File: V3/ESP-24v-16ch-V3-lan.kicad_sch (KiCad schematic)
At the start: 28 parts, among them J7 ETHERNET, U5 LAN8710A

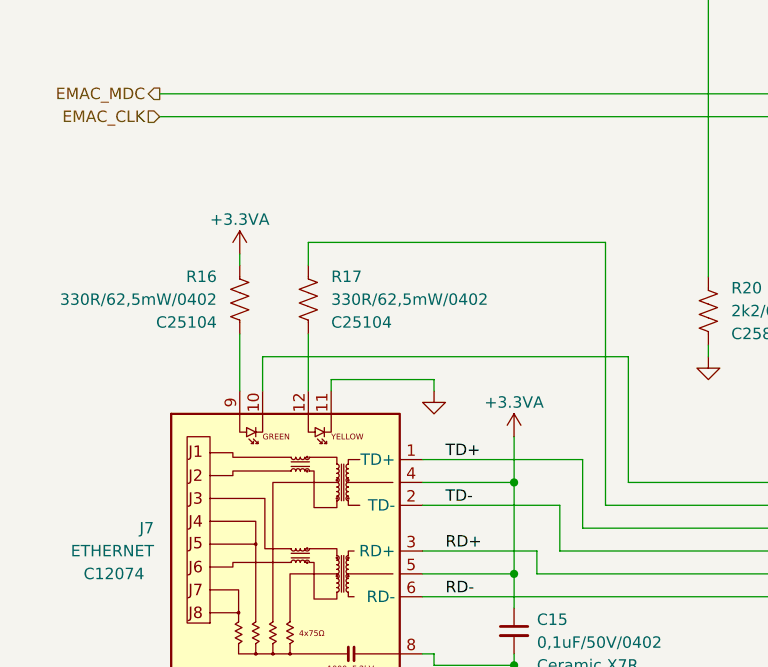
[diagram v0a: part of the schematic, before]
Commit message: Replaced R16 and R17 for a R-Pack
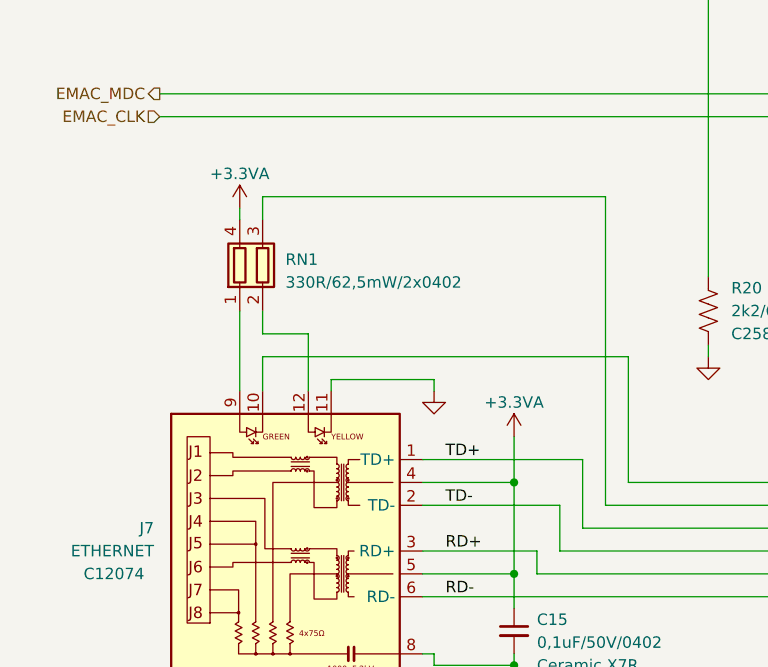
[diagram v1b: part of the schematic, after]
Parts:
- removed R16, R17: 330R/62,5mW/0402, Tales:R_0402_1005Metric, symbol Device:R_US
- added RN1: 330R/62,5mW/2x0402, Resistor_SMD:R_Array_Convex_2x0402, symbol Device:R_Pack02
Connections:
- net +3.3VA: now also RN1.4 (R1.2)
- net LED_Y_A: now also RN1.3 (R2.2)
- net at J7.12: now also RN1.2 (R2.1)
- net at J7.9: now also RN1.1 (R1.1)
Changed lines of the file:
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@@
     (stroke (width 0) (type default))
   )
-  (wire (pts (xy 83.82 123.19) (xy 83.82 152.4))
+  (wire (pts (xy 83.82 118.11) (xy 83.82 152.4))
     (stroke (width 0) (type default))
   )
@@
     (stroke (width 0) (type default))
   )
-  (wire (pts (xy 43.18 124.46) (xy 43.18 125.73))
+  (wire (pts (xy 43.18 119.38) (xy 43.18 120.65))
     (stroke (width 0) (type default))
   )
@@
     (stroke (width 0) (type default))
   )
-  (wire (pts (xy 43.18 133.35) (xy 43.18 139.7))
+  (wire (pts (xy 43.18 130.81) (xy 43.18 139.7))
     (stroke (width 0) (type default))
   )
@@
     (stroke (width 0) (type default))
   )
+  (wire (pts (xy 45.72 133.35) (xy 50.8 133.35))
+    (stroke (width 0) (type default))
+  )
   (wire (pts (xy 151.13 25.4) (xy 151.13 29.21))
     (stroke (width 0) (type default))
@@
     (stroke (width 0) (type default))
   )
+  (wire (pts (xy 45.72 130.81) (xy 45.72 133.35))
+    (stroke (width 0) (type default))
+  )
   (wire (pts (xy 63.5 152.4) (xy 78.74 152.4))
     (stroke (width 0) (type default))
@@
     (stroke (width 0) (type default))
   )
-  (wire (pts (xy 50.8 123.19) (xy 83.82 123.19))
+  (wire (pts (xy 45.72 118.11) (xy 83.82 118.11))
     (stroke (width 0) (type default))
   )
@@
     (stroke (width 0) (type default))
   )
-  (wire (pts (xy 50.8 125.73) (xy 50.8 123.19))
+  (wire (pts (xy 45.72 120.65) (xy 45.72 118.11))
     (stroke (width 0) (type default))
   )
@@
         (path "/2bc5a21a-1d79-419d-a592-6852cc07b00a/c76fc600-a423-4f14-bc69-e86c7c986b21"
           (reference "#PWR060") (unit 1)
-        )
-      )
-    )
-  )
-  (symbol (lib_id "Device:R_US") (at 50.8 129.54 0) (unit 1)
-    (in_bom yes) (on_board yes) (dnp no)
-    (property "Reference" "R17" (at 53.34 127 0)
-      (effects (font (size 1.27 1.27)) (justify left))
-    )
-    (property "Value" "330R/62,5mW/0402" (at 53.34 129.54 0)
-      (effects (font (size 1.27 1.27)) (justify left))
-    )
-    (property "Footprint" "Tales:R_0402_1005Metric" (at 51.816 129.794 90)
-      (effects (font (size 1.27 1.27)) hide)
-    )
-    (property "Datasheet" "~" (at 50.8 129.54 0)
-      (effects (font (size 1.27 1.27)) hide)
-    )
-    (property "Case" "0402/1005" (at 50.8 129.54 0)
-      (effects (font (size 1.27 1.27)) hide)
-    )
-    (property "Mfr" "Uniroyal" (at 50.8 129.54 0)
-      (effects (font (size 1.27 1.27)) hide)
-    )
-    (property "Vendor" "JLCPCB" (at 50.8 129.54 0)
-      (effects (font (size 1.27 1.27)) hide)
-    )
-    (property "Mfr PN" "0402WGF3300TCE" (at 50.8 129.54 0)
-      (effects (font (size 1.27 1.27)) hide)
-    )
-    (property "Technology" "~" (at 50.8 129.54 0)
-      (effects (font (size 1.27 1.27)) hide)
-    )
-    (property "Vendor PN" "C25104" (at 50.8 129.54 0)
-      (effects (font (size 1.27 1.27)) hide)
-    )
-    (property "LCSC Part #" "C25104" (at 53.34 132.08 0)
-      (effects (font (size 1.27 1.27)) (justify left))
-    )
-    (property "JLCPCB BOM" "1" (at 50.8 129.54 0)
-      (effects (font (size 1.27 1.27)) hide)
-    )
-    (pin "1")
-    (pin "2")
-    (instances
-      (project "ESP-24v-16ch-V3"
-        (path "/2bc5a21a-1d79-419d-a592-6852cc07b00a/c76fc600-a423-4f14-bc69-e86c7c986b21"
-          (reference "R17") (unit 1)
         )
       )
@@
     )
   )
-  (symbol (lib_id "Device:R_US") (at 43.18 129.54 0) (unit 1)
-    (in_bom yes) (on_board yes) (dnp no)
-    (property "Reference" "R16" (at 40.64 127 0)
-      (effects (font (size 1.27 1.27)) (justify right))
-    )
-    (property "Value" "330R/62,5mW/0402" (at 40.64 129.54 0)
-      (effects (font (size 1.27 1.27)) (justify right))
-    )
-    (property "Footprint" "Tales:R_0402_1005Metric" (at 44.196 129.794 90)
-      (effects (font (size 1.27 1.27)) hide)
-    )
-    (property "Datasheet" "~" (at 43.18 129.54 0)
-      (effects (font (size 1.27 1.27)) hide)
-    )
-    (property "Case" "0402/1005" (at 43.18 129.54 0)
-      (effects (font (size 1.27 1.27)) hide)
-    )
-    (property "Mfr" "Uniroyal" (at 43.18 129.54 0)
-      (effects (font (size 1.27 1.27)) hide)
-    )
-    (property "Vendor" "JLCPCB" (at 43.18 129.54 0)
-      (effects (font (size 1.27 1.27)) hide)
-    )
-    (property "Mfr PN" "0402WGF3300TCE" (at 43.18 129.54 0)
-      (effects (font (size 1.27 1.27)) hide)
-    )
-    (property "Technology" "~" (at 43.18 129.54 0)
-      (effects (font (size 1.27 1.27)) hide)
-    )
-    (property "Vendor PN" "C25104" (at 43.18 129.54 0)
-      (effects (font (size 1.27 1.27)) hide)
-    )
-    (property "LCSC Part #" "C25104" (at 40.64 132.08 0)
-      (effects (font (size 1.27 1.27)) (justify right))
-    )
-    (property "JLCPCB BOM" "1" (at 43.18 129.54 0)
-      (effects (font (size 1.27 1.27)) hide)
-    )
-    (pin "1")
-    (pin "2")
-    (instances
-      (project "ESP-24v-16ch-V3"
-        (path "/2bc5a21a-1d79-419d-a592-6852cc07b00a/c76fc600-a423-4f14-bc69-e86c7c986b21"
-          (reference "R16") (unit 1)
-        )
-      )
-    )
-  )
   (symbol (lib_id "power:GND") (at 121.92 101.6 0) (unit 1)
     (in_bom yes) (on_board yes) (dnp no)
@@
         (path "/2bc5a21a-1d79-419d-a592-6852cc07b00a/c76fc600-a423-4f14-bc69-e86c7c986b21"
           (reference "#PWR059") (unit 1)
+        )
+      )
+    )
+  )
+  (symbol (lib_id "Device:R_Pack02") (at 45.72 125.73 0) (unit 1)
+    (in_bom yes) (on_board yes) (dnp no) (fields_autoplaced)
+    (property "Reference" "RN1" (at 48.26 125.095 0)
+      (effects (font (size 1.27 1.27)) (justify left))
+    )
+    (property "Value" "330R/62,5mW/2x0402" (at 48.26 127.635 0)
+      (effects (font (size 1.27 1.27)) (justify left))
+    )
+    (property "Footprint" "Resistor_SMD:R_Array_Convex_2x0402" (at 50.165 125.73 90)
+      (effects (font (size 1.27 1.27)) hide)
+    )
+    (property "Datasheet" "~" (at 45.72 125.73 0)
+      (effects (font (size 1.27 1.27)) hide)
+    )
+    (property "Case" "2x0402 Convex" (at 45.72 125.73 0)
+      (effects (font (size 1.27 1.27)) hide)
+    )
+    (property "JLCPCB BOM" "1" (at 45.72 125.73 0)
+      (effects (font (size 1.27 1.27)) hide)
+    )
+    (property "LCSC Part #" "C425334" (at 45.72 125.73 0)
+      (effects (font (size 1.27 1.27)) hide)
+    )
+    (property "Mfr" "Uniroyal" (at 45.72 125.73 0)
+      (effects (font (size 1.27 1.27)) hide)
+    )
+    (property "Mfr PN" "2D02WGJ0331TCE" (at 45.72 125.73 0)
+      (effects (font (size 1.27 1.27)) hide)
+    )
+    (property "Technology" "~" (at 45.72 125.73 0)
+      (effects (font (size 1.27 1.27)) hide)
+    )
+    (property "Vendor" "JLCPCB" (at 45.72 125.73 0)
+      (effects (font (size 1.27 1.27)) hide)
+    )
+    (property "Vendor PN" "C425334" (at 45.72 125.73 0)
+      (effects (font (size 1.27 1.27)) hide)
+    )
+    (pin "1")
+    (pin "2")
+    (pin "3")
+    (pin "4")
+    (instances
+      (project "ESP-24v-16ch-V3"
+        (path "/2bc5a21a-1d79-419d-a592-6852cc07b00a/c76fc600-a423-4f14-bc69-e86c7c986b21"
+          (reference "RN1") (unit 1)
         )
       )
@@
     )
   )
-  (symbol (lib_id "power:+3.3VA") (at 43.18 124.46 0) (unit 1)
-    (in_bom yes) (on_board yes) (dnp no)
-    (property "Reference" "#PWR037" (at 43.18 128.27 0)
-      (effects (font (size 1.27 1.27)) hide)
-    )
-    (property "Value" "+3.3VA" (at 43.18 120.65 0)
+  (symbol (lib_id "power:+3.3VA") (at 43.18 119.38 0) (unit 1)
+    (in_bom yes) (on_board yes) (dnp no)
+    (property "Reference" "#PWR037" (at 43.18 123.19 0)
+      (effects (font (size 1.27 1.27)) hide)
+    )
+    (property "Value" "+3.3VA" (at 43.18 115.57 0)
       (effects (font (size 1.27 1.27)))
     )
-    (property "Footprint" "" (at 43.18 124.46 0)
-      (effects (font (size 1.27 1.27)) hide)
-    )
-    (property "Datasheet" "" (at 43.18 124.46 0)
-      (effects (font (size 1.27 1.27)) hide)
-    )
+    (property "Footprint" "" (at 43.18 119.38 0)
+      (effects (font (size 1.27 1.27)) hide)
+    )
+    (property "Datasheet" "" (at 43.18 119.38 0)
+      (effects (font (size 1.27 1.27)) hide)
+    )
